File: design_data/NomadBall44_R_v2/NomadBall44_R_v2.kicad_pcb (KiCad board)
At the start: 2 copper layers, 147.4 x 96.5 mm, 57 parts, among them SW1 SW_Push, SW10 SW_Push, SW11 SW_Push, SW12 SW_Push, SW13 SW_Push, SW14 SW_Push, SW15 SW_Push, SW16 SW_Push, SW17 SW_Push, SW18 SW_Push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

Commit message: 右手基板のスライドスイッチのGNDパットの位置を変更
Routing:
- net GND: track 182.4 -> 179.3 mm
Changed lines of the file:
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@@
 		)
 		(pad "1" thru_hole oval
-			(at -2.5 1.05 90)
+			(at 2.5 1.05 90)
 			(size 1.3 1)
 			(drill oval 0.8 0.5)
@@
 		)
 		(pad "3" thru_hole oval
-			(at 2.5 1.05 90)
+			(at -2.5 1.05 90)
 			(size 1.3 1)
 			(drill oval 0.8 0.5)
@@
 		)
 		(fp_line
-			(start -0.850001 8.2)
+			(start -0.850003 8.2)
 			(end -0.85 3.6)
 			(stroke
@@
 		(fp_line
 			(start 0.65 8.2)
-			(end 0.649999 3.6)
+			(end 0.649998 3.6)
 			(stroke
 				(width 0.15)
@@
 		)
 		(fp_arc
-			(start -6.305 6.024999)
+			(start -6.305 6.024998)
 			(mid -7.012107 5.732107)
 			(end -7.305 5.025)
@@
 		)
 		(fp_arc
-			(start -4.299999 6.017458)
+			(start -4.299998 6.017458)
 			(mid -3.138277 6.335211)
 			(end -2.3 7.2)
@@
 	)
 	(segment
+		(start 84.87 86.72)
+		(end 85.9 87.75)
+		(width 0.5)
+		(layer "F.Cu")
+		(net 32)
+	)
+	(segment
 		(start 95.45 66.34)
 		(end 92.87 66.34)
@@
 	)
 	(segment
-		(start 85.9 86.04)
-		(end 81.58 81.72)
-		(width 0.5)
-		(layer "F.Cu")
-		(net 32)
-	)
-	(segment
 		(start 94.08 87.75)
 		(end 94.756 88.426)
@@
 	)
 	(segment
-		(start 85.9 87.75)
-		(end 85.9 86.04)
+		(start 81.58 86.72)
+		(end 84.87 86.72)
 		(width 0.5)
 		(layer "F.Cu")

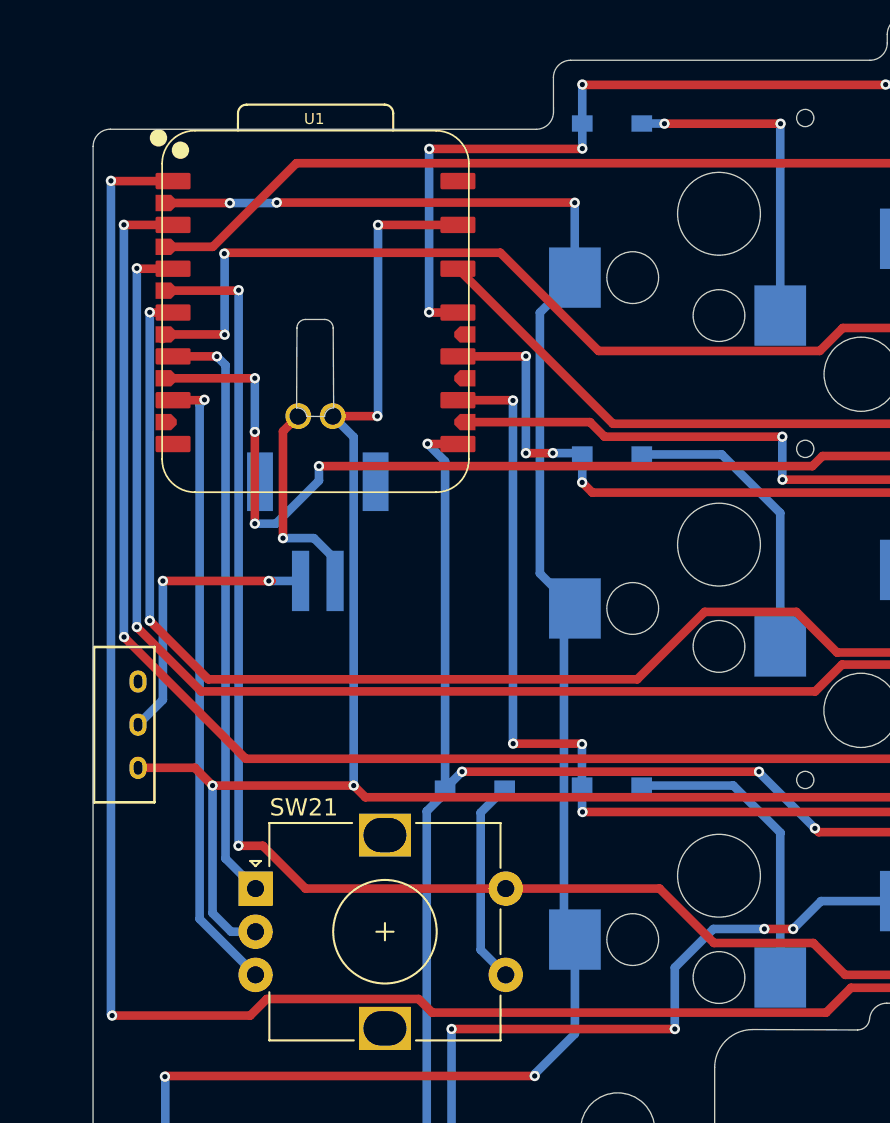
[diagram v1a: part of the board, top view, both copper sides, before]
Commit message: nrf52840 plusのfootprintを変更し配線を修正
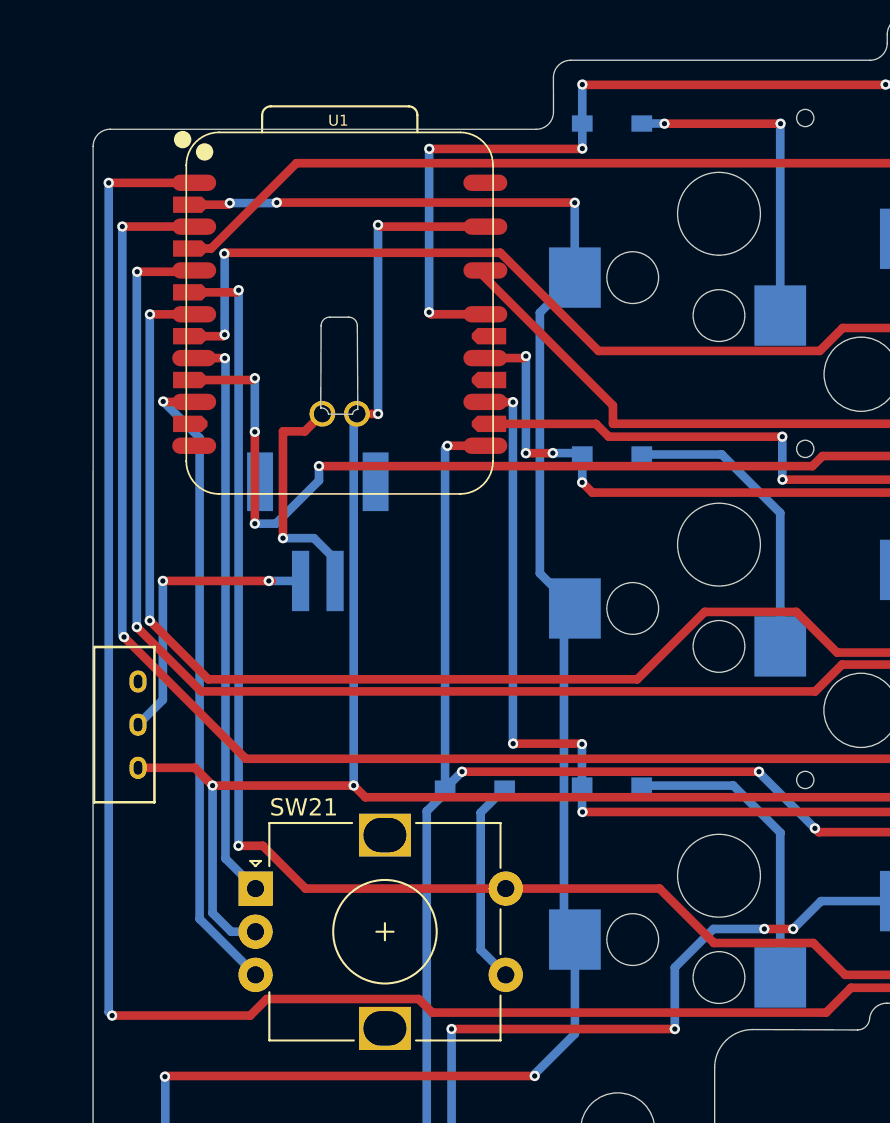
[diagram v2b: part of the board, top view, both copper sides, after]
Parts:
- U1: footprint NomadBall44:XIAO-nRF52840-Plus -> NomadBall44:XIAO-nRF52840-Plus-ver3
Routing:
- net SDIO: track 174.7 -> 176.8 mm
- net SCLK: track 155.1 -> 157.1 mm
- net MOTION: track 170.7 -> 172.6 mm
- net RE_A: track 34.3 -> 32.5 mm
- net CS: track 158.9 -> 160.7 mm
- net Col3: track 174.5 -> 172.8 mm
- net RE_B: track 36.6 -> 38.1 mm
- net Col5: track 160.3 -> 158.8 mm
- net Col1: track 144.7 -> 143.4 mm
- net Col4: track 158.2 -> 156.9 mm
- net Col2: track 144.8 -> 143.5 mm
- net Col0: track 130.4 -> 129.0 mm
- net GND: track 179.3 -> 178.1 mm
- net Row2: track 152.2 -> 151.3 mm
- net Row3: track 186.4 -> 185.6 mm
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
